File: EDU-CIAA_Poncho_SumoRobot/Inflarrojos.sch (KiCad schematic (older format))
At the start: 21 parts, among them P11 CONN_01X02, P12 CONN_01X02, P13 CONN_01X02, P14 CONN_01X02, P15 CONN_01X02, P16 CONN_01X02, P17 CONN_01X02, P18 CONN_01X02, U5 40106

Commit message: Reorganizo bibliotecas en esquemático y PCB. Reparo señal de 12V. Agrego Footprints. Coloco plantilla EDU-CIAA. Reparo asociación conector EDU-CIAA en sch y pcb.
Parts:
- P11, P12, P13, P14, P15, P16, P17, P18: footprint Pin_Headers:Pin_Header_Straight_1x02 -> sumo_robot:Pin_Header_Straight_1x02
- R10, R11, R12, R13, R14, R15, R16, R17, R18, R19, R20, R9: footprint Resistors_ThroughHole:Resistor_Horizontal_RM7mm -> sumo_robot:Resistor_Horizontal_RM7mm
- U5: footprint 40xx:40xx-DIL14 -> sumo_robot:40xx-DIL14
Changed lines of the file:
@@
 EESchema Schematic File Version 2
-LIBS:PONCHO-CIAA-rescue
-LIBS:PONCHO-CIAA-cache
+LIBS:power
+LIBS:PonchoSumoRobot-cache
 EELAYER 25 0
 EELAYER END
@@
 F 0 "R19" V 8680 2600 50  0000 C CNN
 F 1 "220" V 8600 2600 50  0000 C CNN
-F 2 "Resistors_ThroughHole:Resistor_Horizontal_RM7mm" V 8530 2600 50  0001 C CNN
+F 2 "sumo_robot:Resistor_Horizontal_RM7mm" V 8530 2600 50  0001 C CNN
 F 3 "" H 8600 2600 50  0000 C CNN
 	1    8600 2600
@@
 F 0 "R17" V 7730 2600 50  0000 C CNN
 F 1 "220" V 7650 2600 50  0000 C CNN
-F 2 "Resistors_ThroughHole:Resistor_Horizontal_RM7mm" V 7580 2600 50  0001 C CNN
+F 2 "sumo_robot:Resistor_Horizontal_RM7mm" V 7580 2600 50  0001 C CNN
 F 3 "" H 7650 2600 50  0000 C CNN
 	1    7650 2600
@@
 F 0 "R15" V 6730 2600 50  0000 C CNN
 F 1 "220" V 6650 2600 50  0000 C CNN
-F 2 "Resistors_ThroughHole:Resistor_Horizontal_RM7mm" V 6580 2600 50  0001 C CNN
+F 2 "sumo_robot:Resistor_Horizontal_RM7mm" V 6580 2600 50  0001 C CNN
 F 3 "" H 6650 2600 50  0000 C CNN
 	1    6650 2600
@@
 F 0 "R13" V 5780 2600 50  0000 C CNN
 F 1 "220" V 5700 2600 50  0000 C CNN
-F 2 "Resistors_ThroughHole:Resistor_Horizontal_RM7mm" V 5630 2600 50  0001 C CNN
+F 2 "sumo_robot:Resistor_Horizontal_RM7mm" V 5630 2600 50  0001 C CNN
 F 3 "" H 5700 2600 50  0000 C CNN
 	1    5700 2600
@@
 F 0 "R12" V 4780 2600 50  0000 C CNN
 F 1 "180" V 4700 2600 50  0000 C CNN
-F 2 "Resistors_ThroughHole:Resistor_Horizontal_RM7mm" V 4630 2600 50  0001 C CNN
+F 2 "sumo_robot:Resistor_Horizontal_RM7mm" V 4630 2600 50  0001 C CNN
 F 3 "" H 4700 2600 50  0000 C CNN
 	1    4700 2600
@@
 F 0 "R11" V 3780 2600 50  0000 C CNN
 F 1 "180" V 3700 2600 50  0000 C CNN
-F 2 "Resistors_ThroughHole:Resistor_Horizontal_RM7mm" V 3630 2600 50  0001 C CNN
+F 2 "sumo_robot:Resistor_Horizontal_RM7mm" V 3630 2600 50  0001 C CNN
 F 3 "" H 3700 2600 50  0000 C CNN
 	1    3700 2600
@@
 F 0 "R10" V 2780 2600 50  0000 C CNN
 F 1 "180" V 2700 2600 50  0000 C CNN
-F 2 "Resistors_ThroughHole:Resistor_Horizontal_RM7mm" V 2630 2600 50  0001 C CNN
+F 2 "sumo_robot:Resistor_Horizontal_RM7mm" V 2630 2600 50  0001 C CNN
 F 3 "" H 2700 2600 50  0000 C CNN
 	1    2700 2600
@@
 F 0 "R9" V 1830 2600 50  0000 C CNN
 F 1 "180" V 1750 2600 50  0000 C CNN
-F 2 "Resistors_ThroughHole:Resistor_Horizontal_RM7mm" V 1680 2600 50  0001 C CNN
+F 2 "sumo_robot:Resistor_Horizontal_RM7mm" V 1680 2600 50  0001 C CNN
 F 3 "" H 1750 2600 50  0000 C CNN
 	1    1750 2600
@@
 F 0 "P11" H 1950 3150 50  0000 C CNN
 F 1 "CONN_01X02" V 2050 3000 50  0000 C CNN
-F 2 "Pin_Headers:Pin_Header_Straight_1x02" H 1950 3000 50  0001 C CNN
+F 2 "sumo_robot:Pin_Header_Straight_1x02" H 1950 3000 50  0001 C CNN
 F 3 "" H 1950 3000 50  0000 C CNN
 	1    1950 3000
@@
 F 0 "P12" H 2900 3150 50  0000 C CNN
 F 1 "CONN_01X02" V 3000 3000 50  0000 C CNN
-F 2 "Pin_Headers:Pin_Header_Straight_1x02" H 2900 3000 50  0001 C CNN
+F 2 "sumo_robot:Pin_Header_Straight_1x02" H 2900 3000 50  0001 C CNN
 F 3 "" H 2900 3000 50  0000 C CNN
 	1    2900 3000
@@
 F 0 "P13" H 3900 3150 50  0000 C CNN
 F 1 "CONN_01X02" V 4000 3000 50  0000 C CNN
-F 2 "Pin_Headers:Pin_Header_Straight_1x02" H 3900 3000 50  0001 C CNN
+F 2 "sumo_robot:Pin_Header_Straight_1x02" H 3900 3000 50  0001 C CNN
 F 3 "" H 3900 3000 50  0000 C CNN
 	1    3900 3000
@@
 F 0 "P14" H 4900 3150 50  0000 C CNN
 F 1 "CONN_01X02" V 5000 3000 50  0000 C CNN
-F 2 "Pin_Headers:Pin_Header_Straight_1x02" H 4900 3000 50  0001 C CNN
+F 2 "sumo_robot:Pin_Header_Straight_1x02" H 4900 3000 50  0001 C CNN
 F 3 "" H 4900 3000 50  0000 C CNN
 	1    4900 3000
@@
 F 0 "P15" H 5900 3150 50  0000 C CNN
 F 1 "CONN_01X02" V 6000 3000 50  0000 C CNN
-F 2 "Pin_Headers:Pin_Header_Straight_1x02" H 5900 3000 50  0001 C CNN
+F 2 "sumo_robot:Pin_Header_Straight_1x02" H 5900 3000 50  0001 C CNN
 F 3 "" H 5900 3000 50  0000 C CNN
 	1    5900 3000
@@
 F 0 "P16" H 6850 3150 50  0000 C CNN
 F 1 "CONN_01X02" V 6950 3000 50  0000 C CNN
-F 2 "Pin_Headers:Pin_Header_Straight_1x02" H 6850 3000 50  0001 C CNN
+F 2 "sumo_robot:Pin_Header_Straight_1x02" H 6850 3000 50  0001 C CNN
 F 3 "" H 6850 3000 50  0000 C CNN
 	1    6850 3000
@@
 F 0 "P17" H 7850 3150 50  0000 C CNN
 F 1 "CONN_01X02" V 7950 3000 50  0000 C CNN
-F 2 "Pin_Headers:Pin_Header_Straight_1x02" H 7850 3000 50  0001 C CNN
+F 2 "sumo_robot:Pin_Header_Straight_1x02" H 7850 3000 50  0001 C CNN
 F 3 "" H 7850 3000 50  0000 C CNN
 	1    7850 3000
@@
 F 0 "P18" H 8800 3150 50  0000 C CNN
 F 1 "CONN_01X02" V 8900 3000 50  0000 C CNN
-F 2 "Pin_Headers:Pin_Header_Straight_1x02" H 8800 3000 50  0001 C CNN
+F 2 "sumo_robot:Pin_Header_Straight_1x02" H 8800 3000 50  0001 C CNN
 F 3 "" H 8800 3000 50  0000 C CNN
 	1    8800 3000
@@
 F 0 "R20" V 8680 3450 50  0000 C CNN
 F 1 "10K" V 8600 3450 50  0000 C CNN
-F 2 "Resistors_ThroughHole:Resistor_Horizontal_RM7mm" V 8530 3450 50  0001 C CNN
+F 2 "sumo_robot:Resistor_Horizontal_RM7mm" V 8530 3450 50  0001 C CNN
 F 3 "" H 8600 3450 50  0000 C CNN
 	1    8600 3450
@@
 F 0 "R18" V 7730 3450 50  0000 C CNN
 F 1 "10K" V 7650 3450 50  0000 C CNN
-F 2 "Resistors_ThroughHole:Resistor_Horizontal_RM7mm" V 7580 3450 50  0001 C CNN
+F 2 "sumo_robot:Resistor_Horizontal_RM7mm" V 7580 3450 50  0001 C CNN
 F 3 "" H 7650 3450 50  0000 C CNN
 	1    7650 3450
@@
 F 0 "R16" V 6730 3450 50  0000 C CNN
 F 1 "10K" V 6650 3450 50  0000 C CNN
-F 2 "Resistors_ThroughHole:Resistor_Horizontal_RM7mm" V 6580 3450 50  0001 C CNN
+F 2 "sumo_robot:Resistor_Horizontal_RM7mm" V 6580 3450 50  0001 C CNN
 F 3 "" H 6650 3450 50  0000 C CNN
 	1    6650 3450
@@
 F 0 "R14" V 5780 3450 50  0000 C CNN
 F 1 "10K" V 5700 3450 50  0000 C CNN
-F 2 "Resistors_ThroughHole:Resistor_Horizontal_RM7mm" V 5630 3450 50  0001 C CNN
+F 2 "sumo_robot:Resistor_Horizontal_RM7mm" V 5630 3450 50  0001 C CNN
 F 3 "" H 5700 3450 50  0000 C CNN
 	1    5700 3450
@@
 F 0 "U5" H 6250 3900 50  0000 L CNN
 F 1 "40106" H 6200 3600 50  0000 L CNN
-F 2 "40xx:40xx-DIL14" H 6150 3750 60  0001 C CNN
+F 2 "sumo_robot:40xx-DIL14" H 6150 3750 60  0001 C CNN
 F 3 "" H 6150 3750 60  0000 C CNN
 	1    6150 3750
@@
 F 0 "U5" H 7200 3900 50  0000 L CNN
 F 1 "40106" H 7150 3600 50  0000 L CNN
-F 2 "40xx:40xx-DIL14" H 7100 3750 60  0001 C CNN
+F 2 "sumo_robot:40xx-DIL14" H 7100 3750 60  0001 C CNN
 F 3 "" H 7100 3750 60  0000 C CNN
 	2    7100 3750
@@
 F 0 "U5" H 8200 3900 50  0000 L CNN
 F 1 "40106" H 8150 3600 50  0000 L CNN
-F 2 "40xx:40xx-DIL14" H 8100 3750 60  0001 C CNN
+F 2 "sumo_robot:40xx-DIL14" H 8100 3750 60  0001 C CNN
 F 3 "" H 8100 3750 60  0000 C CNN
 	3    8100 3750
@@
 F 0 "U5" H 9150 3900 50  0000 L CNN
 F 1 "40106" H 9100 3600 50  0000 L CNN
-F 2 "40xx:40xx-DIL14" H 9050 3750 60  0001 C CNN
+F 2 "sumo_robot:40xx-DIL14" H 9050 3750 60  0001 C CNN
 F 3 "" H 9050 3750 60  0000 C CNN
 	4    9050 3750

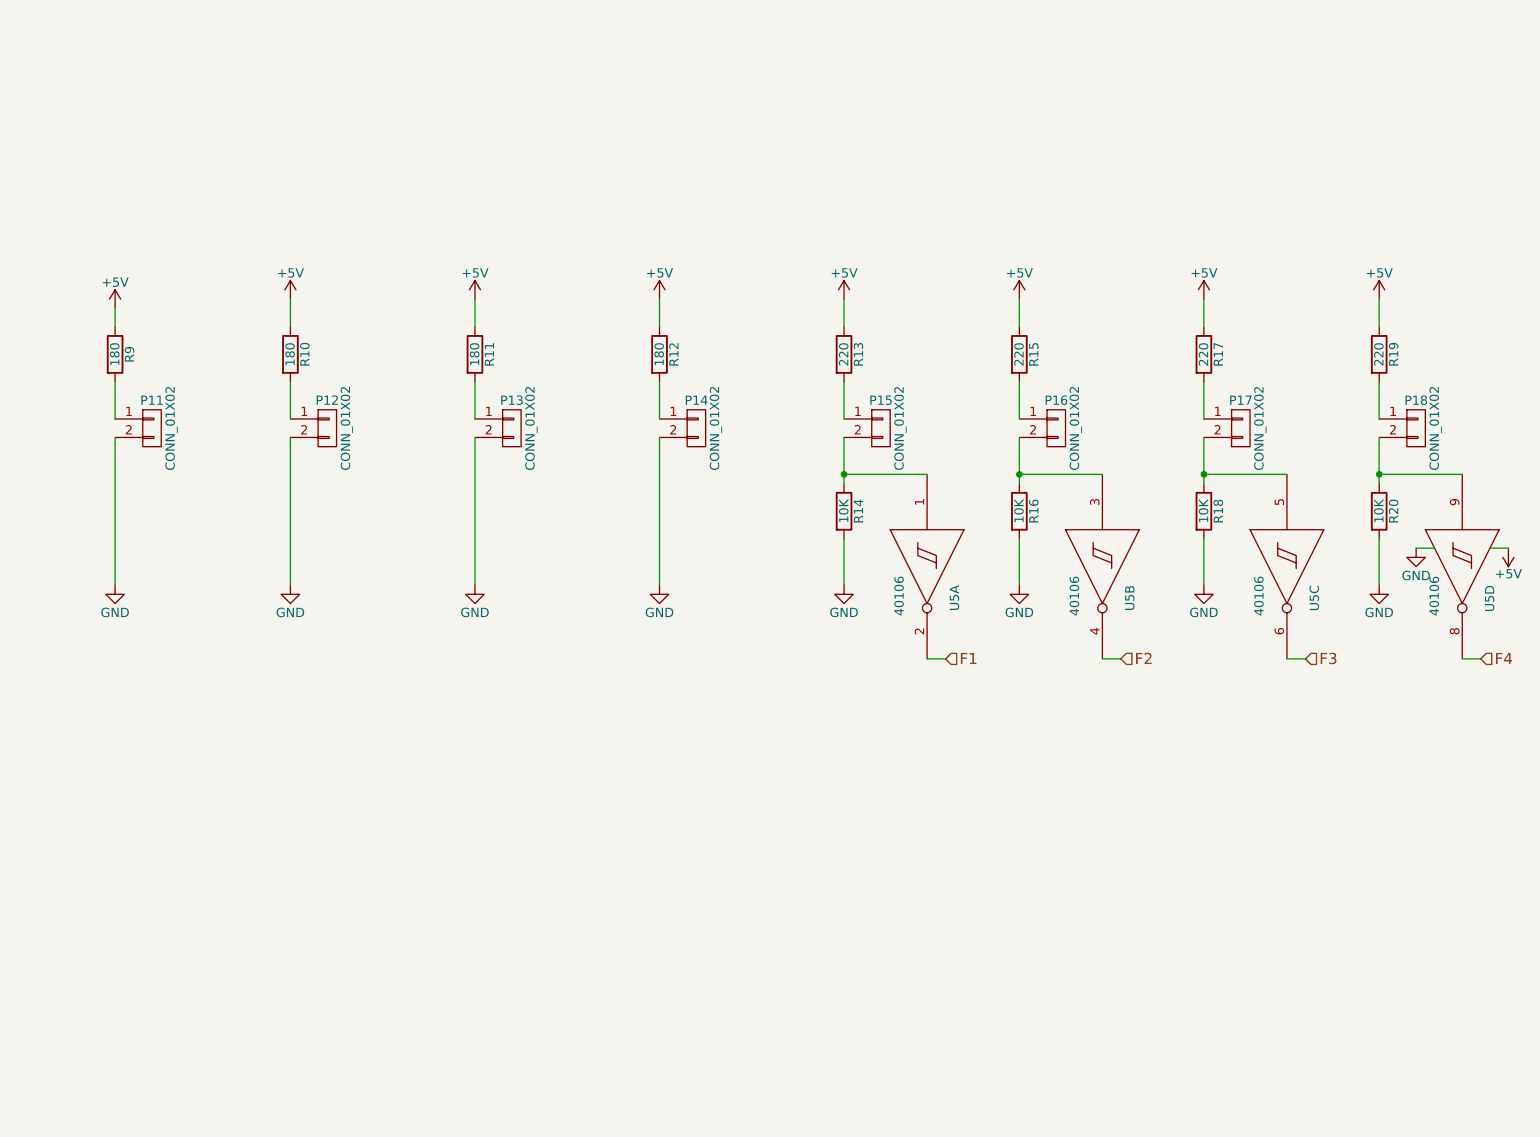
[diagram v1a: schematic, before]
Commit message: Correcciones propuestas al Poncho SumoRobot.
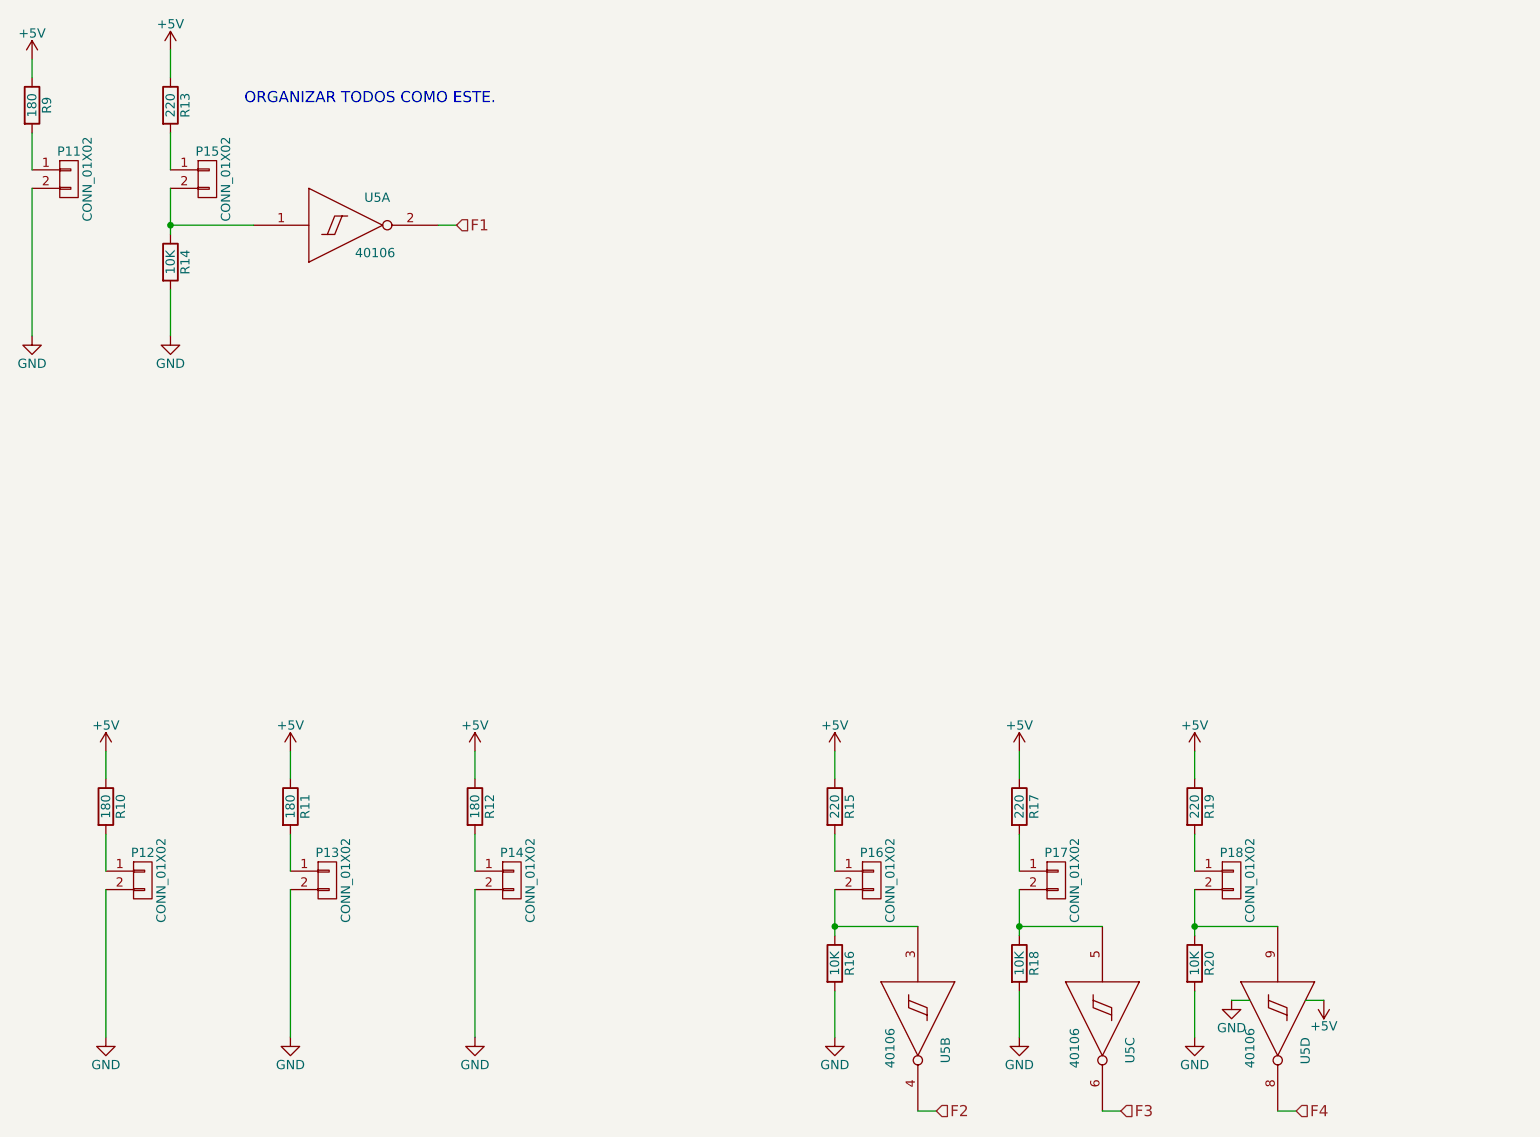
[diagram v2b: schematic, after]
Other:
- note added: "ORGANIZAR TODOS COMO ESTE."
- moved on the sheet: P11, P12, P13, P14, P15, P16, P17, P18, R10, R11, R12, R13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

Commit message: Actualizo trabajo del Poncho Sumo Robot.
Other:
- note removed: "ORGANIZAR TODOS COMO ESTE."
- moved on the sheet: P12, P13, P14, P16, P17, P18, R10, R11, R12, R15, R16, R17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
